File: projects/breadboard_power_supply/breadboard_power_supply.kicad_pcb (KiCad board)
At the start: 2 copper layers, 17 parts, among them J1 Barrel_Jack_Switch, J2 Conn_01x03_Pin, J3 Conn_01x02_Pin, J4 Screw_Terminal_01x02, J5 Conn_01x03_Pin, J6 Screw_Terminal_01x02, J7 Conn_01x02_Pin, U1 LM317_TO-220, U2 LM7805_TO220

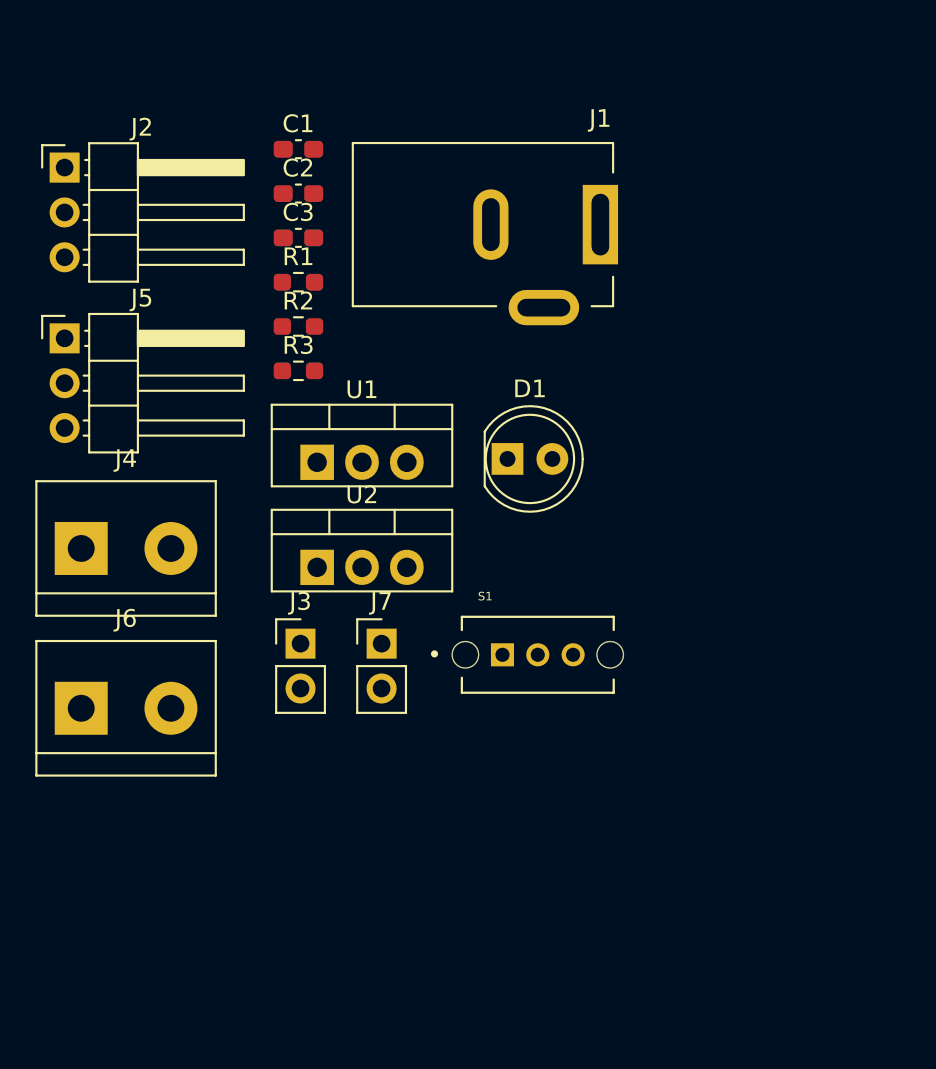
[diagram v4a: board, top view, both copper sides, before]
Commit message: Finish breadboard_power_supply projeect in v1
Finish PCB design
Correct design issues in schematic and PCB: separate power_output nets A and B,
rewire accordingly
Add silkscreen text and decorations
Improve 3D
Improve notes
Add figures
Generate gerbers
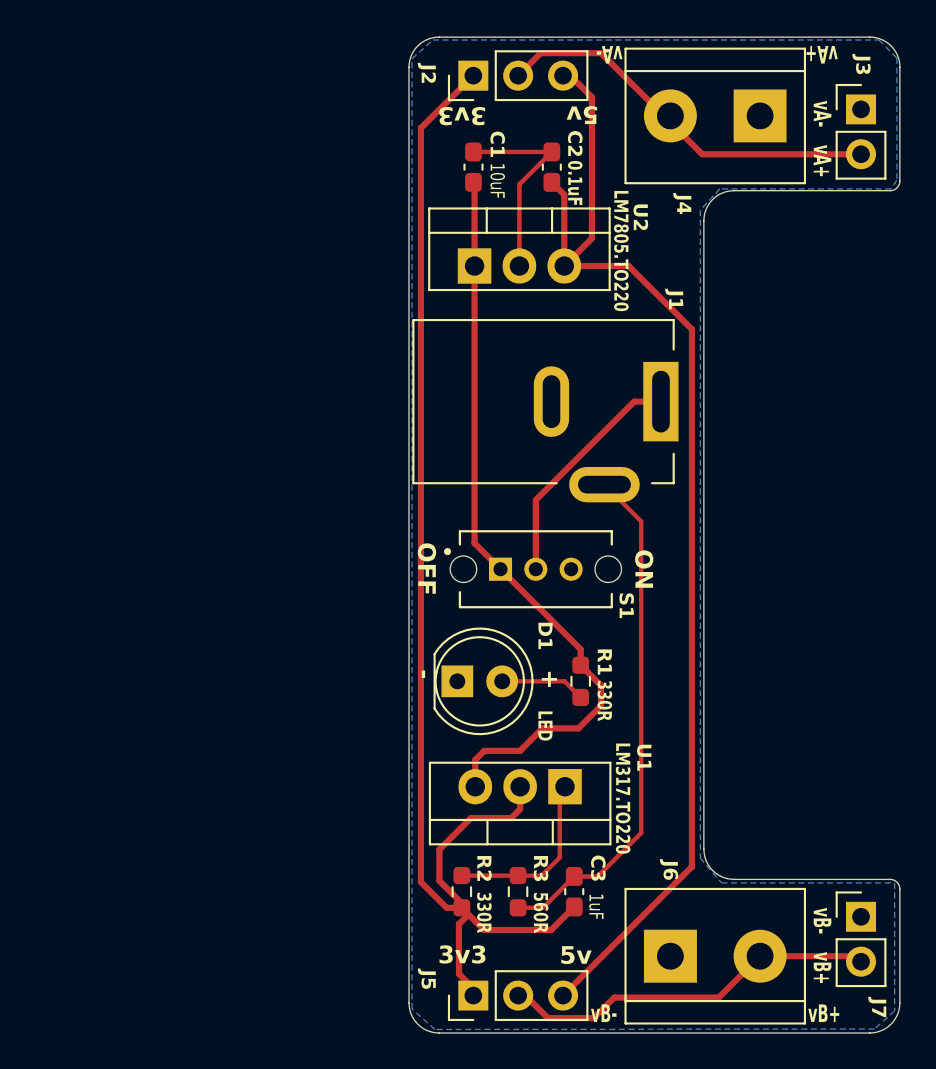
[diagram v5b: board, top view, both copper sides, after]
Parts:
- added G***: LOGO, MH_Logo:robot_duckie_logo_10mm, B.Cu at (141.0, 102.2)
- added REF**: KiCad-Logo2_5mm_SilkScreen, Symbol:KiCad-Logo2_5mm_SilkScreen, B.Cu at (133.3, 87.6)
- C1: value 10 uF -> 10uF
- C2: value 0.1 uF -> 0.1uF
- C3: value 1 uF -> 1uF
- J2, J5: footprint Connector_PinHeader_2.54mm:PinHeader_1x03_P2.54mm_Horizontal -> Connector_PinHeader_2.54mm:PinHeader_1x03_P2.54mm_Vertical
- R1, R2: value 330 Ohms -> 330R
- R3: value 560 Ohms -> 560R
- U1: value LM317_TO-220 -> LM317.TO220
- U2: value LM7805_TO220 -> LM7805.TO220
- moved J4 45.6 mm to (149.6, 70.5), turned to 180 degrees
- moved J3 43.8 mm to (155.3, 70.1)
- moved J5 43.8 mm to (133.3, 120.3), turned to 90 degrees
- moved C3 40.2 mm to (139.1, 114.4), turned to -90 degrees
- moved J6 36.2 mm to (144.5, 118.1)
- moved R2 33.3 mm to (132.7, 114.4), turned to -90 degrees
- moved R3 32.0 mm to (135.9, 114.4), turned to 90 degrees
- moved J7 31.2 mm to (155.3, 115.8)
- moved R1 27.7 mm to (139.4, 102.5), turned to -90 degrees
- moved J2 23.7 mm to (133.3, 68.2), turned to 90 degrees
- moved U1 23.1 mm to (138.5, 108.5), turned to 180 degrees
- moved U2 19.3 mm to (133.4, 79.0)
- moved C2 14.4 mm to (137.8, 73.4), turned to -90 degrees
- moved D1 12.9 mm to (132.4, 102.5)
- moved J1 10.6 mm to (144.0, 86.7)
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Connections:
- J2 pad 2: /PWR_output -> /PWR_output_A
- J3 pad 2: /PWR_output -> /PWR_output_A
- J4 pad 2: /PWR_output -> /PWR_output_A
- J5 pad 2: /PWR_output -> /PWR_output_B
- J6 pad 2: /PWR_output -> /PWR_output_B
- J7 pad 2: /PWR_output -> /PWR_output_B
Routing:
- net /3.3V: track 0.00 -> 73.6 mm
- net /5V: track 0.00 -> 66.5 mm
- net /12V: track 0.00 -> 42.5 mm
- net GND: track 0.00 -> 41.0 mm
- net /PWR_output_A: track 0.00 -> 22.3 mm
- net /PWR_output_B: track 0.00 -> 21.1 mm
- net /PWR_input: track 0.00 -> 14.8 mm
- net Net-(U1-ADJ): track 0.00 -> 10.1 mm
- net Net-(D1-A): track 0.00 -> 4.82 mm
- added copper zone on B.Cu, net GND
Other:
- board outline added: 27.8 x 56.4 mm
- board text added: "+"
- board text added: "-"
- board text added: "3v3"
- board text added: "5v"
- board text added: "Breadboard power supply v1.0"
- board text added: "OFF"
- board text added: "ON"
- board text added: "vA+"
- board text added: "vA-"
- board text added: "vB+"
- board text added: "vB-"

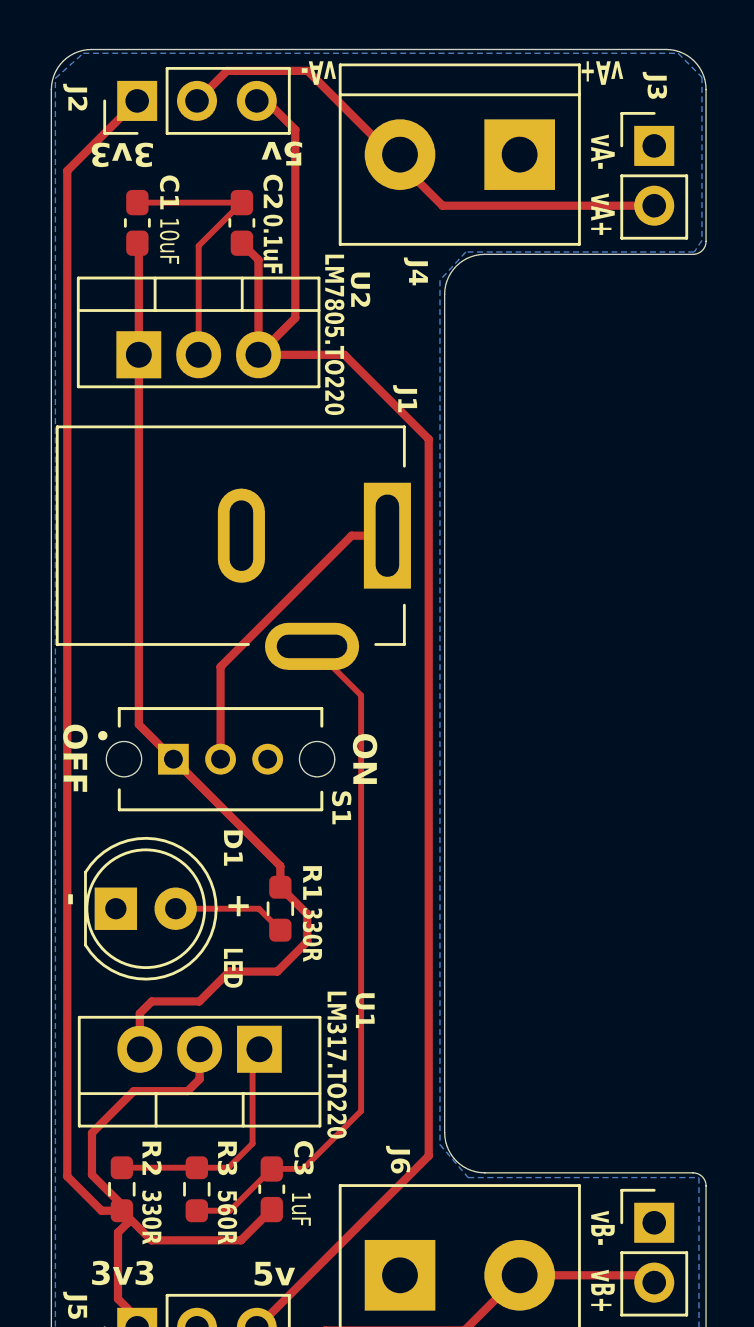
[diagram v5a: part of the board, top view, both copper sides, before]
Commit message: breadboard power supply version v2.0
Changes in v2.0 (Dec'25):

- fix errors:
  - flip Switch S1 (so OFF and ON work as intended)
  - flip J4 Screw Terminal (so vA+ and vA- are as intended)

- update schematics:
  - improve readability
  - update version number to v2.0

- update silkscreen:
  - Update version number in back silkscreen to v2.0
  - fix footprint of J4 screw terminal in front silkscreen

- update 3D view:
  - color mask black
  - add jumpers

Update text and figures in README.md
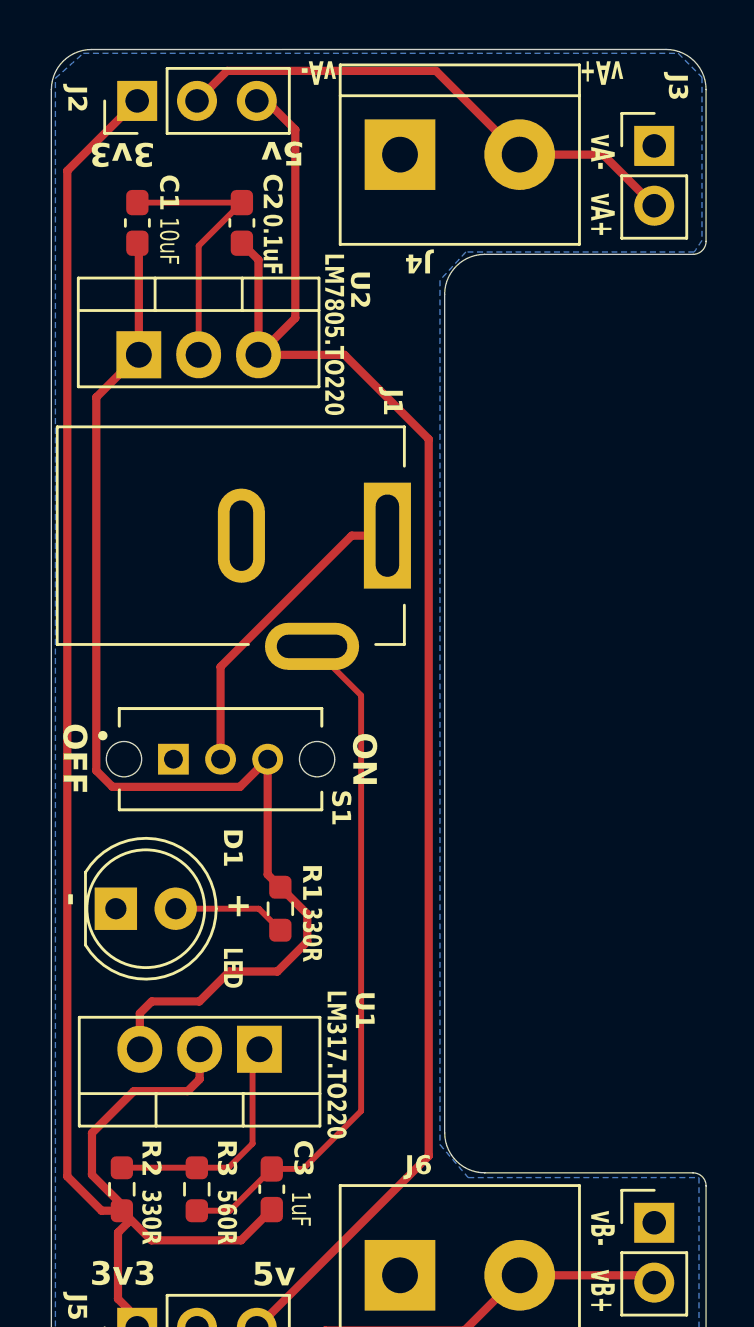
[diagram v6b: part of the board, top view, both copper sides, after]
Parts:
- moved J4 5.08 mm to (144.5, 70.5), turned to 0 degrees
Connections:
- S1 pad 1: /12V -> unconnected-(S1-Pad1)
- S1 pad 3: unconnected-(S1-Pad3) -> /12V
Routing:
- net /12V: track 42.5 -> 49.6 mm
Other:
- board text added: "Breadboard power supply v2.0"
- board text removed: "Breadboard power supply v1.0"
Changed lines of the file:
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@@
 	(net 7 "/PWR_output_A")
 	(net 8 "Net-(U1-ADJ)")
-	(net 9 "unconnected-(S1-Pad3)")
+	(net 9 "unconnected-(S1-Pad1)")
 	(net 10 "/PWR_output_B")
 	(footprint "Connector_BarrelJack:BarrelJack_Kycon_KLDX-0202-xC_Horizontal"
@@
 		(tags "power jack 2mm 2.5mm KLDX-0202-BC KLDX-0202-AC")
 		(property "Reference" "J1"
-			(at 0.83 -5.745 270)
+			(at 0.225 -5.665 270)
 			(unlocked yes)
 			(layer "F.SilkS")
@@
 	(footprint "TerminalBlock:TerminalBlock_bornier-2_P5.08mm"
 		(layer "F.Cu")
-		(at 149.59 70.485 180)
+		(at 144.51 70.485)
 		(descr "simple 2-pin terminal block, pitch 5.08mm, revamped version of bornier2")
 		(tags "terminal block bornier2")
 		(property "Reference" "J4"
-			(at 4.325 -5.015 270)
+			(at 0.79 4.615 180)
 			(unlocked yes)
 			(layer "F.SilkS")
@@
 		)
 		(property "Value" "Screw_Terminal_01x02"
-			(at -6.71 -5.315 0)
+			(at 11.49 5.215 0)
 			(layer "F.Fab")
 			(effects
@@
 		)
 		(property "Datasheet" "~"
-			(at 0 0 180)
+			(at 0 0 0)
 			(unlocked yes)
 			(layer "F.Fab")
@@
 		)
 		(property "Description" "Generic screw terminal, single row, 01x02, script generated (kicad-library-utils/schlib/autogen/connector/)"
-			(at 0 0 180)
+			(at 0 0 0)
 			(unlocked yes)
 			(layer "F.Fab")
@@
 		)
 		(property "My_Label" "JUMP WIRES OUTPUT A"
-			(at 0 0 180)
+			(at 0 0 0)
 			(unlocked yes)
 			(layer "F.Fab")
@@
 		(attr through_hole)
 		(fp_line
-			(start 7.62 3.81)
-			(end 7.62 -3.81)
+			(start -2.54 -3.81)
+			(end -2.54 3.81)
 			(stroke
 				(width 0.12)
@@
 		)
 		(fp_line
-			(start 7.62 2.54)
-			(end -2.54 2.54)
+			(start -2.54 3.81)
+			(end 7.62 3.81)
 			(stroke
 				(width 0.12)
@@
 		)
 		(fp_line
-			(start -2.54 3.81)
-			(end 7.62 3.81)
+			(start 7.62 -2.5)
+			(end -2.54 -2.5)
 			(stroke
 				(width 0.12)
@@
 		)
 		(fp_line
-			(start -2.54 -3.81)
-			(end -2.54 3.81)
+			(start 7.62 3.81)
+			(end 7.62 -3.81)
 			(stroke
 				(width 0.12)
@@
 		)
 		(fp_line
-			(start 7.79 4)
-			(end 7.79 -4)
+			(start -2.71 -4)
+			(end -2.71 4)
 			(stroke
 				(width 0.05)
@@
 		)
 		(fp_line
-			(start 7.79 4)
-			(end -2.71 4)
+			(start -2.71 -4)
+			(end 7.79 -4)
 			(stroke
 				(width 0.05)
@@
 		)
 		(fp_line
-			(start -2.71 -4)
-			(end 7.79 -4)
+			(start 7.79 4)
+			(end -2.71 4)
 			(stroke
 				(width 0.05)
@@
 		)
 		(fp_line
-			(start -2.71 -4)
-			(end -2.71 4)
+			(start 7.79 4)
+			(end 7.79 -4)
 			(stroke
 				(width 0.05)
@@
 		)
 		(fp_line
-			(start 7.54 3.75)
-			(end 7.54 -3.75)
+			(start -2.46 -3.75)
+			(end -2.46 3.75)
 			(stroke
 				(width 0.1)
@@
 		)
 		(fp_line
-			(start 7.54 -3.75)
-			(end -2.46 -3.75)
+			(start -2.46 3.75)
+			(end 7.54 3.75)
 			(stroke
 				(width 0.1)
@@
 		)
 		(fp_line
-			(start -2.46 3.75)
-			(end 7.54 3.75)
+			(start 7.54 -3.75)
+			(end -2.46 -3.75)
 			(stroke
 				(width 0.1)
@@
 		)
 		(fp_line
-			(start -2.46 -3.75)
-			(end -2.46 3.75)
+			(start 7.54 3.75)
+			(end 7.54 -3.75)
 			(stroke
 				(width 0.1)
@@
 		)
 		(fp_text user "${REFERENCE}"
-			(at 2.54 0 0)
+			(at 1.59 0.515 0)
 			(layer "F.Fab")
 			(effects
 				(font
 					(size 1 1)
-					(thickness 0.15)
+					(thickness 0.125)
 				)
+				(justify left bottom)
 			)
 		)
 		(pad "1" thru_hole rect
-			(at 0 0 180)
+			(at 0 0)
 			(size 3 3)
 			(drill 1.52)
@@
 		)
 		(pad "2" thru_hole circle
-			(at 5.08 0 180)
+			(at 5.08 0)
 			(size 3 3)
 			(drill 1.52)
@@
 			)
 			(rotate
-				(xyz -90 -0 -0)
+				(xyz -90 -0 -180)
 			)
 		)
@@
 		(tags "terminal block bornier2")
 		(property "Reference" "J6"
-			(at -0.005 -4.85 270)
+			(at 0.79 -4.67 0)
 			(unlocked yes)
 			(layer "F.SilkS")
@@
 			(layers "*.Cu" "*.Mask")
 			(remove_unused_layers no)
-			(net 2 "/12V")
+			(net 9 "unconnected-(S1-Pad1)")
 			(pinfunction "1")
-			(pintype "passive")
+			(pintype "passive+no_connect")
 			(solder_mask_margin 0.102)
 		)
@@
 			(layers "*.Cu" "*.Mask")
 			(remove_unused_layers no)
-			(net 9 "unconnected-(S1-Pad3)")
+			(net 2 "/12V")
 			(pinfunction "3")
-			(pintype "passive+no_connect")
+			(pintype "passive")
 			(solder_mask_margin 0.102)
 		)
@@
 		(tags "Through hole pin header THT 1x02 2.54mm single row")
 		(property "Reference" "J3"
-			(at 0.1 -2.495 270)
+			(at 1 -2.495 270)
 			(unlocked yes)
 			(layer "F.SilkS")
@@
 			)
 		)
+		(model "${KIPRJMOD}/libraries/MH_Jumper/jumper-2-54mm-pitch-1.snapshot.19/Jumpers/Jumper-yellow.step"
+			(offset
+				(xyz 0 -3.8 0.5)
+			)
+			(scale
+				(xyz 1 1 1)
+			)
+			(rotate
+				(xyz -0 -0 -90)
+			)
+		)
 	)
 	(footprint "Connector_PinHeader_2.54mm:PinHeader_1x03_P2.54mm_Vertical"
@@
 			)
 		)
+		(model "${KIPRJMOD}/libraries/MH_Jumper/jumper-2-54mm-pitch-1.snapshot.19/Jumpers/Jumper-yellow.step"
+			(offset
+				(xyz 0 -3.8 0)
+			)
+			(scale
+				(xyz 1 1 1)
+			)
+			(rotate
+				(xyz -0 -0 -90)
+			)
+		)
 	)
 	(footprint "Package_TO_SOT_THT:TO-220-3_Vertical"
@@
 		)
 	)
-	(gr_text "Breadboard power supply\nv1.0"
+	(gr_text "Breadboard power supply\nv2.0"
 		(at 139.505 89.32 270)
 		(layer "B.SilkS")
@@
 	)
 	(segment
-		(start 133.42 78.985)
-		(end 133.42 94.685)
+		(start 133.42 74.309603)
+		(end 133.42 78.985)
 		(width 0.35)
 		(layer "F.Cu")
@@
 	)
 	(segment
-		(start 133.42 74.309603)
-		(end 133.42 78.985)
+		(start 135.993 106.442)
+		(end 133.969 106.442)
 		(width 0.35)
 		(layer "F.Cu")
@@
 	)
 	(segment
-		(start 139.43 100.695)
-		(end 139.43 101.5925)
+		(start 133.35853 74.248133)
+		(end 133.42 74.309603)
 		(width 0.35)
 		(layer "F.Cu")
@@
 	)
 	(segment
-		(start 135.993 106.442)
-		(end 133.969 106.442)
+		(start 138.89 96.155)
+		(end 138.89 101.0525)
 		(width 0.35)
 		(layer "F.Cu")
@@
 	)
 	(segment
-		(start 133.35853 74.248133)
-		(end 133.42 74.309603)
+		(start 131.614 96.642115)
+		(end 131.614 80.791)
+		(width 0.35)
+		(layer "F.Cu")
+		(net 2)
+	)
+	(segment
+		(start 131.614 80.791)
+		(end 133.42 78.985)
 		(width 0.35)
 		(layer "F.Cu")
@@
 	)
 	(segment
-		(start 133.42 94.685)
-		(end 134.89 96.155)
+		(start 137.714 97.331)
+		(end 132.302885 97.331)
+		(width 0.35)
+		(layer "F.Cu")
+		(net 2)
+	)
+	(segment
+		(start 138.89 101.0525)
+		(end 139.43 101.5925)
 		(width 0.35)
 		(layer "F.Cu")
@@
 	)
 	(segment
+		(start 138.89 96.155)
+		(end 137.714 97.331)
+		(width 0.35)
+		(layer "F.Cu")
+		(net 2)
+	)
+	(segment
 		(start 140.573 103.902)
 		(end 139.303 105.172)
@@
 	)
 	(segment
-		(start 134.89 96.155)
-		(end 139.43 100.695)
+		(start 140.573 102.7355)
+		(end 140.573 103.902)
 		(width 0.35)
 		(layer "F.Cu")
@@
 	)
 	(segment
-		(start 140.573 102.7355)
-		(end 140.573 103.902)
+		(start 132.302885 97.331)
+		(end 131.614 96.642115)
 		(width 0.35)
 		(layer "F.Cu")
@@
 	)
 	(segment
-		(start 137.166 66.929)
-		(end 140.589 66.929)
+		(start 153.135 70.485)
+		(end 155.305 72.655)
 		(width 0.35)
 		(layer "F.Cu")
@@
 	)
 	(segment
-		(start 146.315 72.655)
-		(end 155.305 72.655)
+		(start 135.89 68.205)
+		(end 137.166 66.929)
 		(width 0.35)
 		(layer "F.Cu")
@@
 	)
 	(segment
-		(start 135.89 68.205)
-		(end 137.166 66.929)
+		(start 149.59 70.485)
+		(end 153.135 70.485)
 		(width 0.35)
 		(layer "F.Cu")
@@
 	)
 	(segment
-		(start 144.145 70.485)
-		(end 146.315 72.655)
+		(start 146.034 66.929)
+		(end 149.59 70.485)
 		(width 0.35)
 		(layer "F.Cu")
@@
 	)
 	(segment
-		(start 140.589 66.929)
-		(end 144.145 70.485)
+		(start 137.166 66.929)
+		(end 146.034 66.929)
 		(width 0.35)
 		(layer "F.Cu")
